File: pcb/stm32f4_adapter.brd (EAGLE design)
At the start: 58.4 x 119 mm, 2 parts

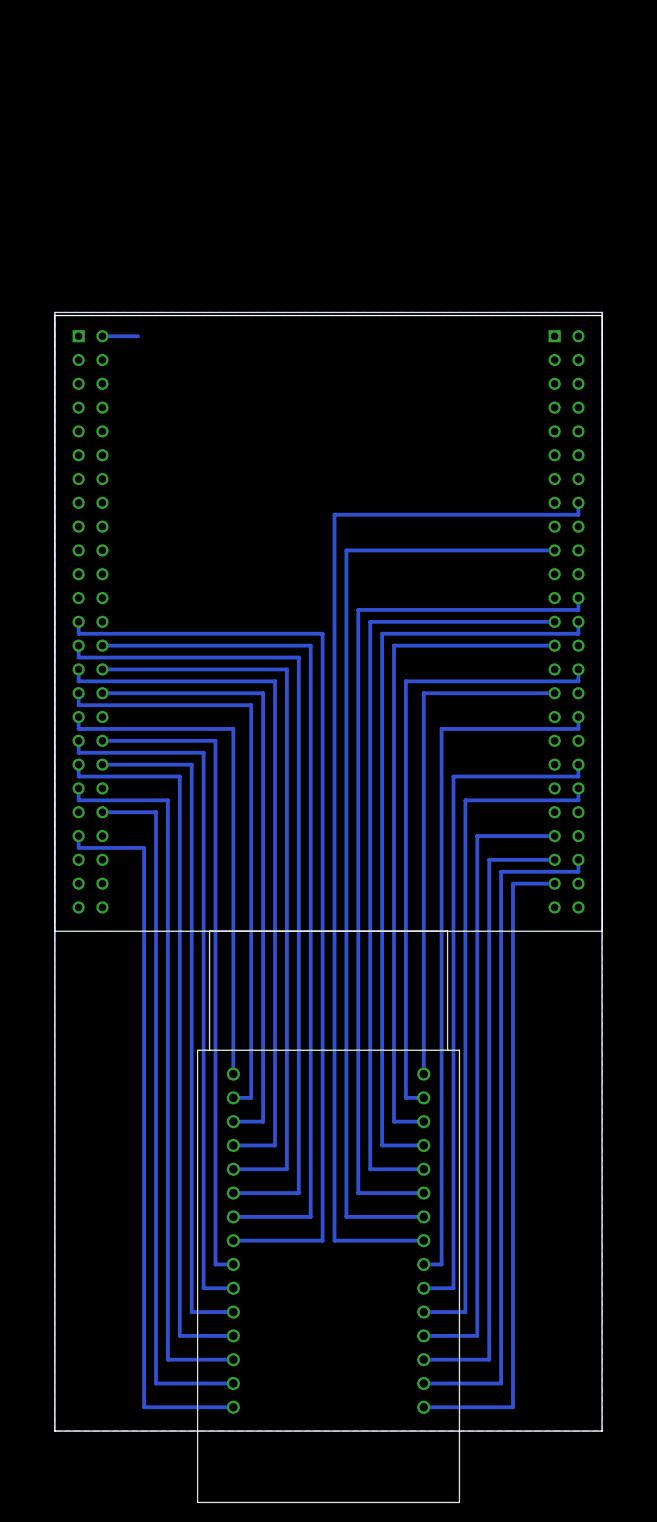
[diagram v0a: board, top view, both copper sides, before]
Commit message: Move pin E3 to E2, because E3 is used by CS_I2C/SPI!
For Rev. 2. the STM32F4 Discovery datasheet is lying!
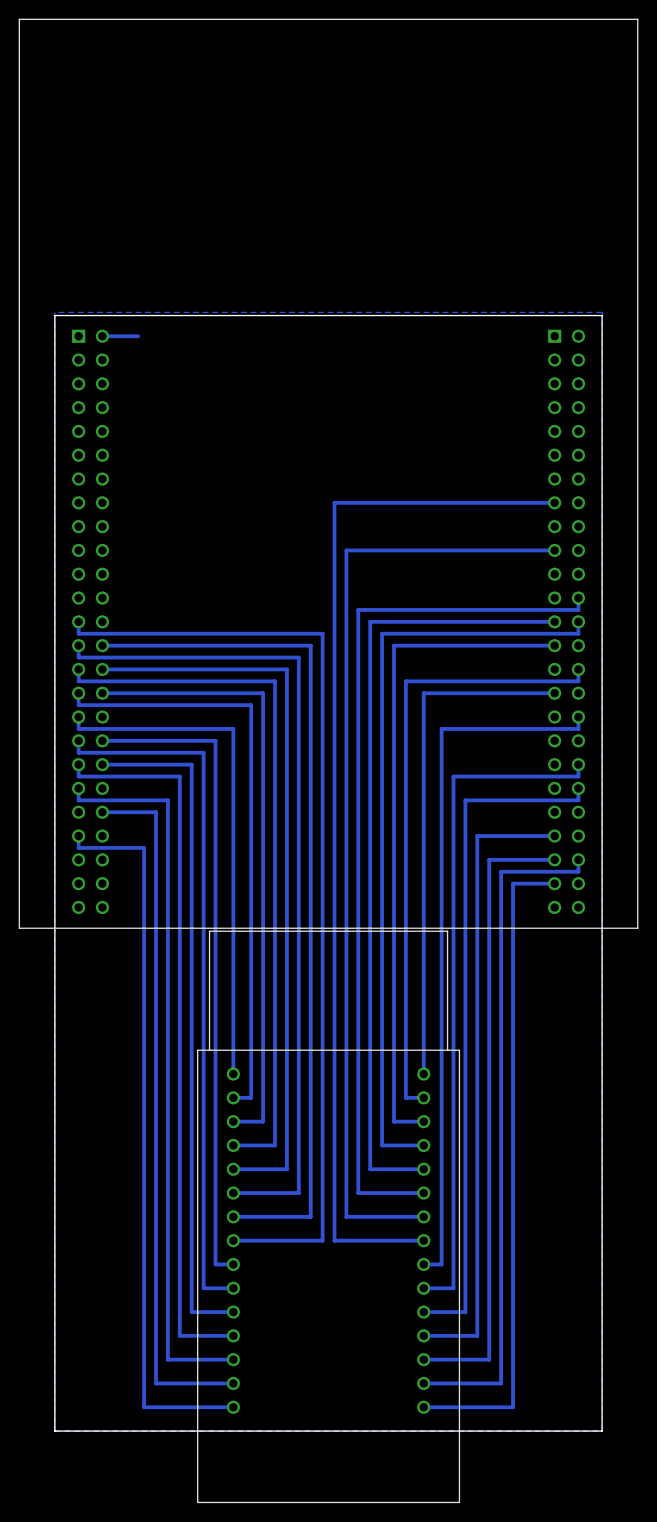
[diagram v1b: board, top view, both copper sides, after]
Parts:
- U$1: device STM32F4-DISCOVERY:STM32F4-DISCOVERY -> elva:STM32F4-DISCOVERY
- moved U$1 1.27 mm to (29.2, 86.4)
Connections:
- removed net N$30: U$1.P$66, U$2.P$8
- new net N$23: U$1.P$65, U$2.P$8
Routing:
- net N$30: track 114.3 -> 0.00 mm
- net N$23: track 0.00 -> 111.8 mm
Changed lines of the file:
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@@
 </autorouter>
 <elements>
-<element name="U$1" library="STM32F4-DISCOVERY" package="STM32F4-DISCOVERY" value="STM32F4-DISCOVERY" x="30.48" y="86.36"/>
+<element name="U$1" library="elva" package="STM32F4-DISCOVERY" value="STM32F4-DISCOVERY" x="29.21" y="86.36"/>
 <element name="U$2" library="STM32F4-DISCOVERY" package="IPOD-CONNECTOR" value="IPOD-CONNECTOR" x="29.21" y="20.32"/>
 </elements>
@@
 <wire x1="31.115" y1="93.98" x2="53.34" y2="93.98" width="0.4064" layer="16"/>
 </signal>
-<signal name="N$30">
-<contactref element="U$1" pad="P$66"/>
-<contactref element="U$2" pad="P$8"/>
-<wire x1="39.37" y1="20.32" x2="29.845" y2="20.32" width="0.4064" layer="16"/>
-<wire x1="29.845" y1="20.32" x2="29.845" y2="97.79" width="0.4064" layer="16"/>
-<wire x1="29.845" y1="97.79" x2="55.88" y2="97.79" width="0.4064" layer="16"/>
-<wire x1="55.88" y1="97.79" x2="55.88" y2="99.06" width="0.4064" layer="16"/>
-</signal>
 <signal name="N$31">
 <contactref element="U$1" pad="P$81"/>
@@
 <wire x1="5.08" y1="116.84" x2="8.89" y2="116.84" width="0.4064" layer="16"/>
 </signal>
+<signal name="N$23">
+<contactref element="U$1" pad="P$65"/>
+<contactref element="U$2" pad="P$8"/>
+<wire x1="39.37" y1="20.32" x2="29.845" y2="20.32" width="0.4064" layer="16"/>
+<wire x1="29.845" y1="20.32" x2="29.845" y2="99.06" width="0.4064" layer="16"/>
+<wire x1="29.845" y1="99.06" x2="53.34" y2="99.06" width="0.4064" layer="16"/>
+</signal>
 </signals>
